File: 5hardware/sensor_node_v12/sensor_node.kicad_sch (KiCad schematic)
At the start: 38 parts, among them J1 Conn_01x08_Socket, J2 Conn_01x08_Socket, Q2 AO3401A, Q3 MMBT5551L, Q4 AO3401A, SW2 SW_Push, SW4 SW_Reed, SW5 SW_Push, SW6 SW_Push, U1 ESP-12F, U12 APDS-9960, U13 SHT31-DIS, U17 BH1750FVI-TR, U2 2N7002DW, U4 CH32V003F4P6, U7 XC6206PxxxMR, U8 TPL5110

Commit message: did some works.
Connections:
- net +3.3V: now also J2.3 (Pin_3); no longer J2.4 (Pin_4)
- net D15: now also J2.4 (Pin_4)
- no-connect marks 24 -> 23
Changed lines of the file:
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@@
   (junction (at 76.2 108.585) (diameter 0) (color 0 0 0 0)
   )
-  (junction (at 62.865 192.405) (diameter 0) (color 0 0 0 0)
+  (junction (at 62.865 189.865) (diameter 0) (color 0 0 0 0)
   )
   (junction (at 317.5 95.885) (diameter 0) (color 0 0 0 0)
@@
   (no_connect (at 240.665 184.15))
   (no_connect (at 243.205 184.15))
-  (no_connect (at 77.47 189.865))
   (no_connect (at 149.86 203.835))
   (no_connect (at 256.54 226.06))
@@
   (no_connect (at 226.06 236.22))
   (no_connect (at 245.745 184.15))
-  (wire (pts (xy 51.435 189.23) (xy 51.435 192.405))
+  (wire (pts (xy 51.435 186.69) (xy 51.435 189.865))
     (stroke (width 0) (type default))
   )
@@
     (stroke (width 0) (type default))
   )
+  (wire (pts (xy 77.47 192.405) (xy 69.215 192.405))
+    (stroke (width 0) (type default))
+  )
   (wire (pts (xy 74.295 184.785) (xy 77.47 184.785))
     (stroke (width 0) (type default))
@@
     (stroke (width 0) (type default))
   )
-  (wire (pts (xy 62.865 192.405) (xy 77.47 192.405))
+  (wire (pts (xy 62.865 189.865) (xy 77.47 189.865))
     (stroke (width 0) (type default))
   )
@@
     (stroke (width 0) (type default))
   )
-  (wire (pts (xy 62.865 189.23) (xy 62.865 192.405))
+  (wire (pts (xy 62.865 186.69) (xy 62.865 189.865))
     (stroke (width 0) (type default))
   )
@@
     (stroke (width 0) (type default))
   )
-  (wire (pts (xy 62.865 192.405) (xy 51.435 192.405))
+  (wire (pts (xy 62.865 189.865) (xy 51.435 189.865))
     (stroke (width 0) (type default))
   )
@@
     (effects (font (size 1.27 1.27)) (justify right))
     (property "Intersheetrefs" "${INTERSHEET_REFS}" (at 135.8379 193.675 0)
+      (effects (font (size 1.27 1.27)) (justify right) hide)
+    )
+  )
+  (global_label "D15" (shape input) (at 69.215 192.405 180) (fields_autoplaced)
+    (effects (font (size 1.27 1.27)) (justify right))
+    (property "Intersheetrefs" "${INTERSHEET_REFS}" (at 62.5408 192.405 0)
       (effects (font (size 1.27 1.27)) (justify right) hide)
     )
@@
     )
   )
-  (symbol (lib_id "power:PWR_FLAG") (at 62.865 189.23 0) (mirror y) (unit 1)
-    (in_bom yes) (on_board yes) (dnp no)
-    (property "Reference" "#FLG04" (at 62.865 187.325 0)
-      (effects (font (size 1.27 1.27)) hide)
-    )
-    (property "Value" "PWR_FLAG" (at 62.865 184.785 0)
-      (effects (font (size 1.27 1.27)))
-    )
-    (property "Footprint" "" (at 62.865 189.23 0)
-      (effects (font (size 1.27 1.27)) hide)
-    )
-    (property "Datasheet" "~" (at 62.865 189.23 0)
+  (symbol (lib_id "power:PWR_FLAG") (at 62.865 186.69 0) (mirror y) (unit 1)
+    (in_bom yes) (on_board yes) (dnp no)
+    (property "Reference" "#FLG04" (at 62.865 184.785 0)
+      (effects (font (size 1.27 1.27)) hide)
+    )
+    (property "Value" "PWR_FLAG" (at 62.865 182.245 0)
+      (effects (font (size 1.27 1.27)))
+    )
+    (property "Footprint" "" (at 62.865 186.69 0)
+      (effects (font (size 1.27 1.27)) hide)
+    )
+    (property "Datasheet" "~" (at 62.865 186.69 0)
       (effects (font (size 1.27 1.27)) hide)
     )
@@
     )
   )
-  (symbol (lib_id "power:+3.3V") (at 51.435 189.23 0) (mirror y) (unit 1)
-    (in_bom yes) (on_board yes) (dnp no)
-    (property "Reference" "#PWR010" (at 51.435 193.04 0)
-      (effects (font (size 1.27 1.27)) hide)
-    )
-    (property "Value" "+3.3V" (at 51.435 185.42 0)
-      (effects (font (size 1.27 1.27)))
-    )
-    (property "Footprint" "" (at 51.435 189.23 0)
-      (effects (font (size 1.27 1.27)) hide)
-    )
-    (property "Datasheet" "" (at 51.435 189.23 0)
-      (effects (font (size 1.27 1.27)) hide)
-    )
+  (symbol (lib_id "power:+3.3V") (at 51.435 186.69 0) (mirror y) (unit 1)
+    (in_bom yes) (on_board yes) (dnp no)
+    (property "Reference" "#PWR010" (at 51.435 190.5 0)
+      (effects (font (size 1.27 1.27)) hide)
+    )
+    (property "Value" "+3.3V" (at 51.435 182.88 0)
+      (effects (font (size 1.27 1.27)))
+    )
+    (property "Footprint" "" (at 51.435 186.69 0)
+      (effects (font (size 1.27 1.27)) hide)
+    )
+    (property "Datasheet" "" (at 51.435 186.69 0)
+      (effects (font (size 1.27 1.27)) hide)
+    )

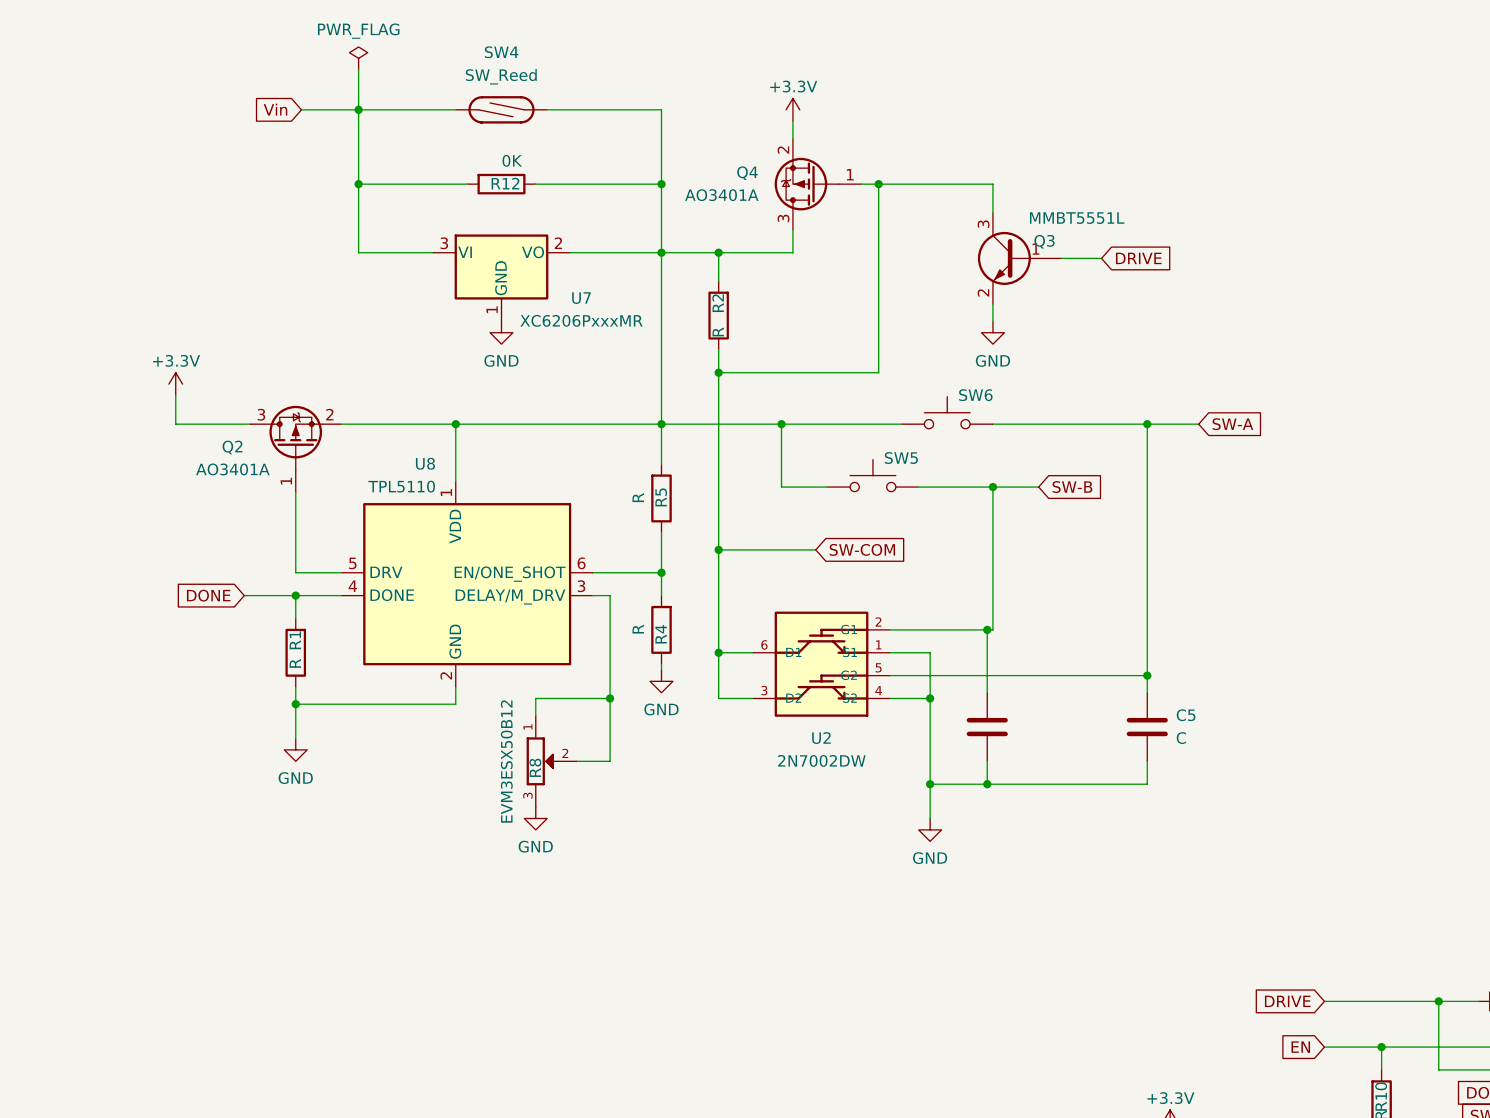
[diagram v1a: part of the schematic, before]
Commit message: update schematic.
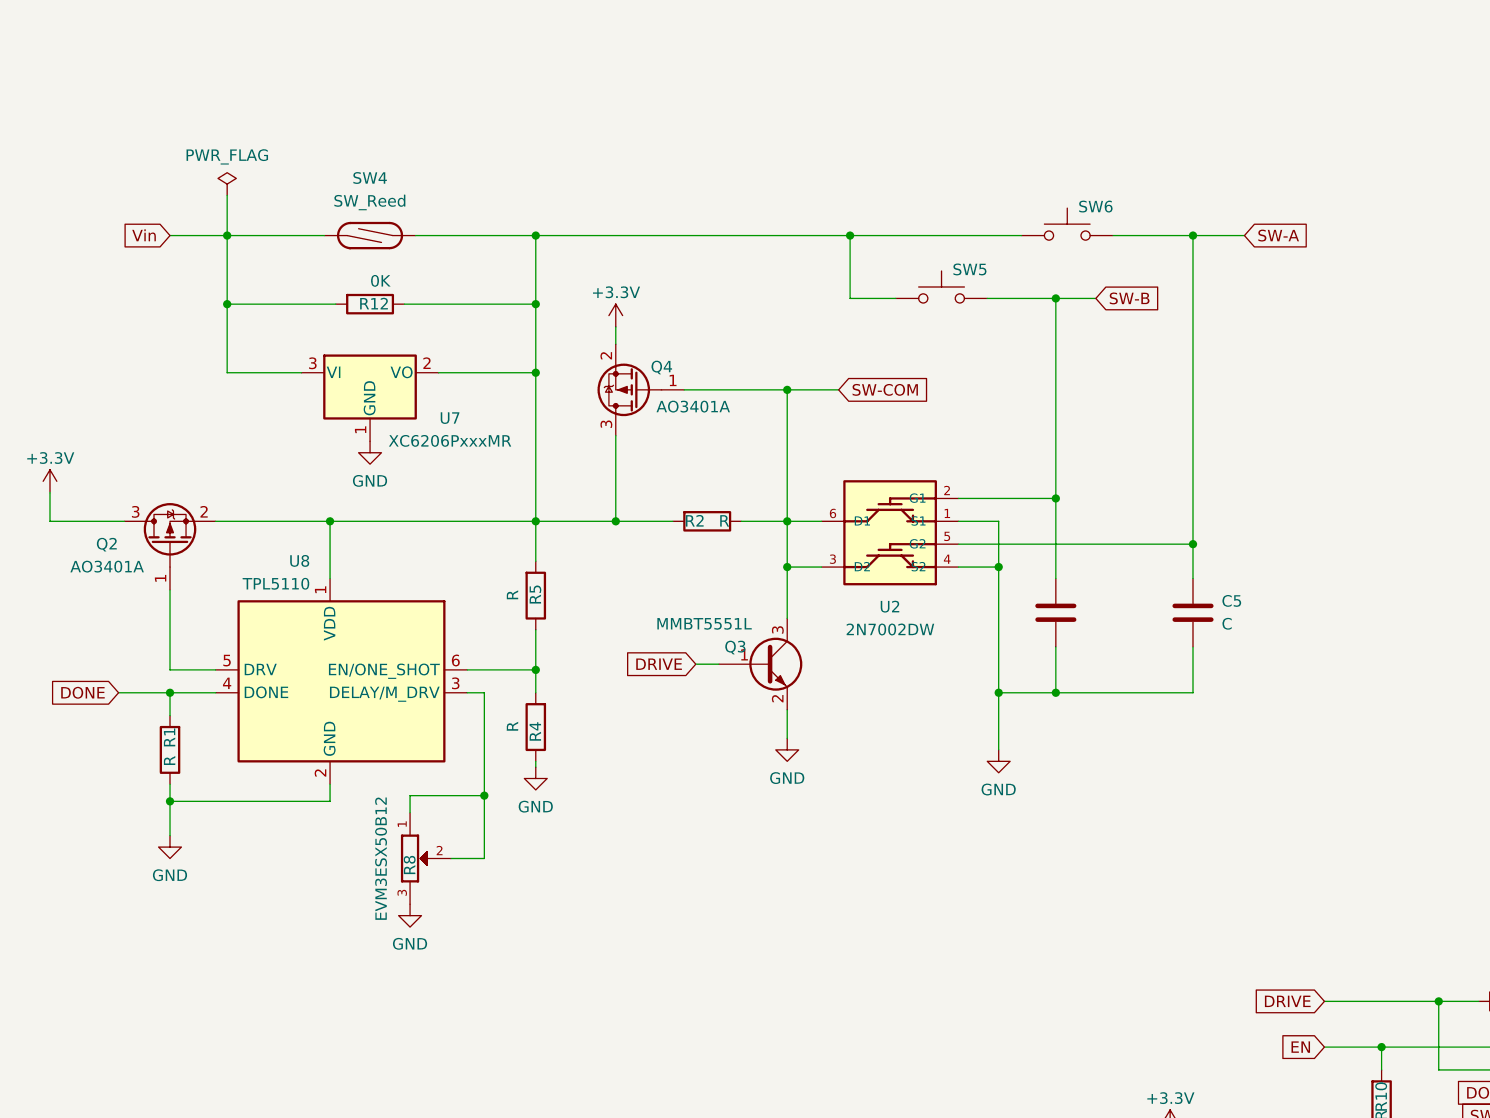
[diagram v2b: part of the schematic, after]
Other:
- moved on the sheet: C5, Q2, Q3, Q4, R1, R12, R2, R4, R5, R8, SW4, SW5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
